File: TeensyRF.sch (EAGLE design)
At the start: 9 parts, among them X1 SMA-142-0701-801/806, X2 SMA-142-0701-801/806

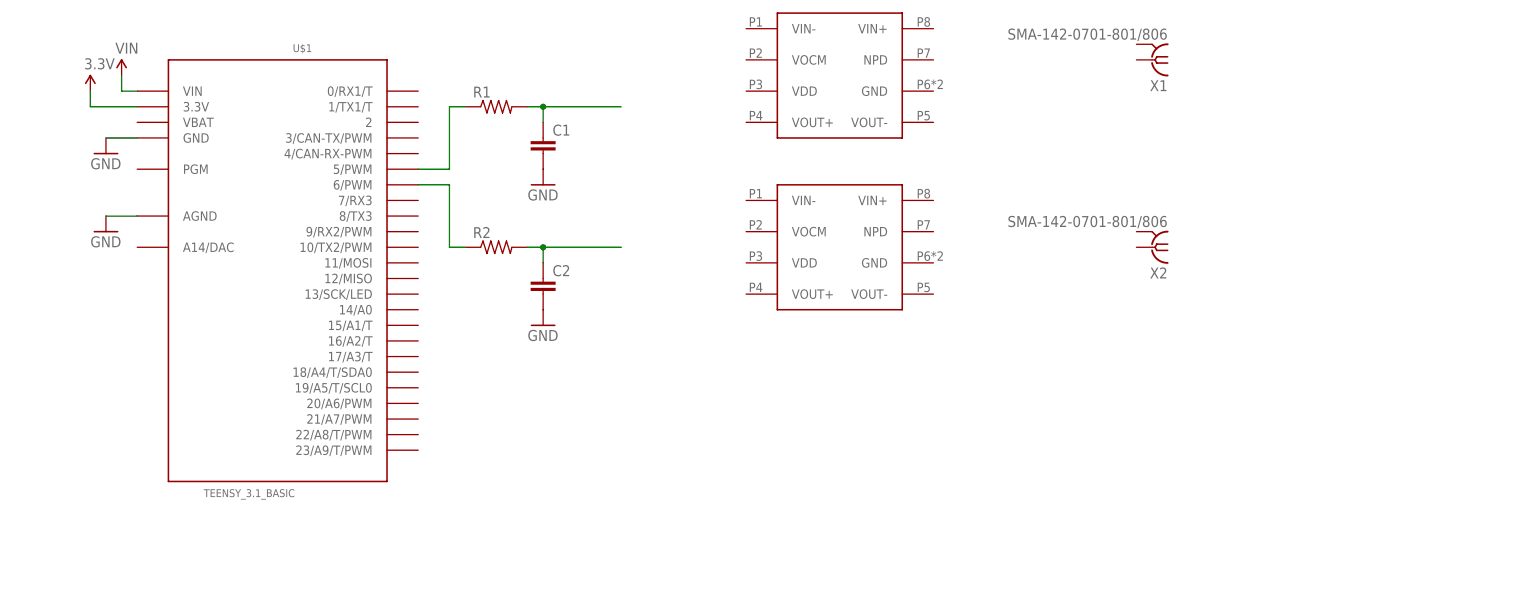
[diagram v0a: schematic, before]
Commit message: Finished TX schematic
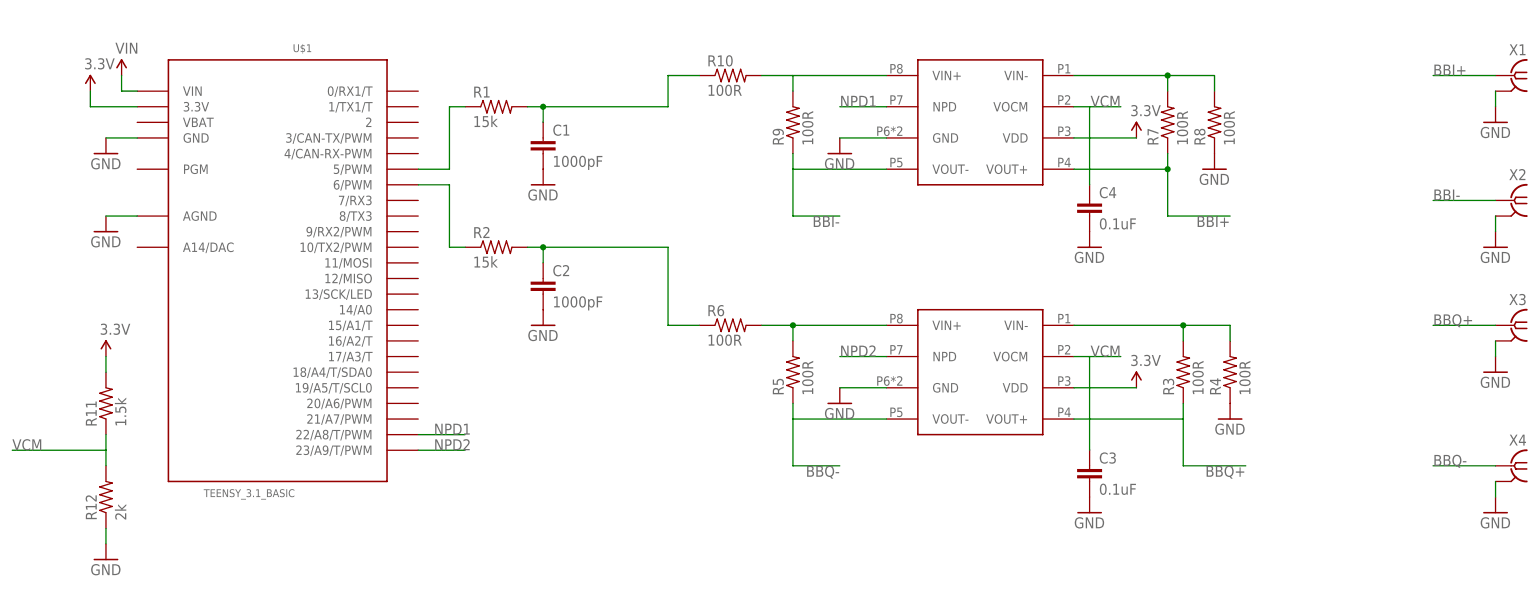
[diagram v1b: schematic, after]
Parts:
- added C3, C4: 0.1uF, SparkFun-Capacitors:CAP0805
- added R10, R3, R4, R5, R6, R7, R8, R9: 100R, SparkFun-Resistors:RESISTOR0805-RES
- added R11: 1.5k, SparkFun-Resistors:RESISTOR0805-RES
- added R12: 2k, SparkFun-Resistors:RESISTOR0805-RES
- added X3, X4: SMA-142-0701-801/806, con-coax:SMA-142-0701-801/806
- C1, C2: value (none) -> 1000pF
- R1, R2: value (none) -> 15k
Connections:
- new net BBI+: R7.1, U$2.VOUT+, X1.1
- new net BBI-: R9.1, U$2.VOUT-, X2.1
- new net BBQ+: R3.1, U$3.VOUT+, X3.1
- new net BBQ-: R5.1, U$3.VOUT-, X4.1
- new net N$11: R7.2, R8.2, U$2.VIN-
- new net N$13: R10.2, R9.2, U$2.VIN+
- new net N$6: R5.2, R6.2, U$3.VIN+
- new net N$8: R3.2, R4.2, U$3.VIN-
- new net NPD1: U$1.22/A8/T/PWM, U$2.NPD
- new net NPD2: U$1.23/A9/T/PWM, U$3.NPD
- new net VCM: C3.1, C4.1, R11.1, R12.2, U$2.VOCM, U$3.VOCM
- net 3.3V: now also R11.2, U$2.VDD, U$3.VDD
- net GND: now also C3.2, C4.2, R12.1, R4.1, R8.1, U$2.GND, U$3.GND, X1.2, X2.2, X3.2, X4.2
- net N$2: now also R10.1
- net N$4: now also R6.1
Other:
- moved on the sheet: X1, X2

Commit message: Finished TX Test board layout
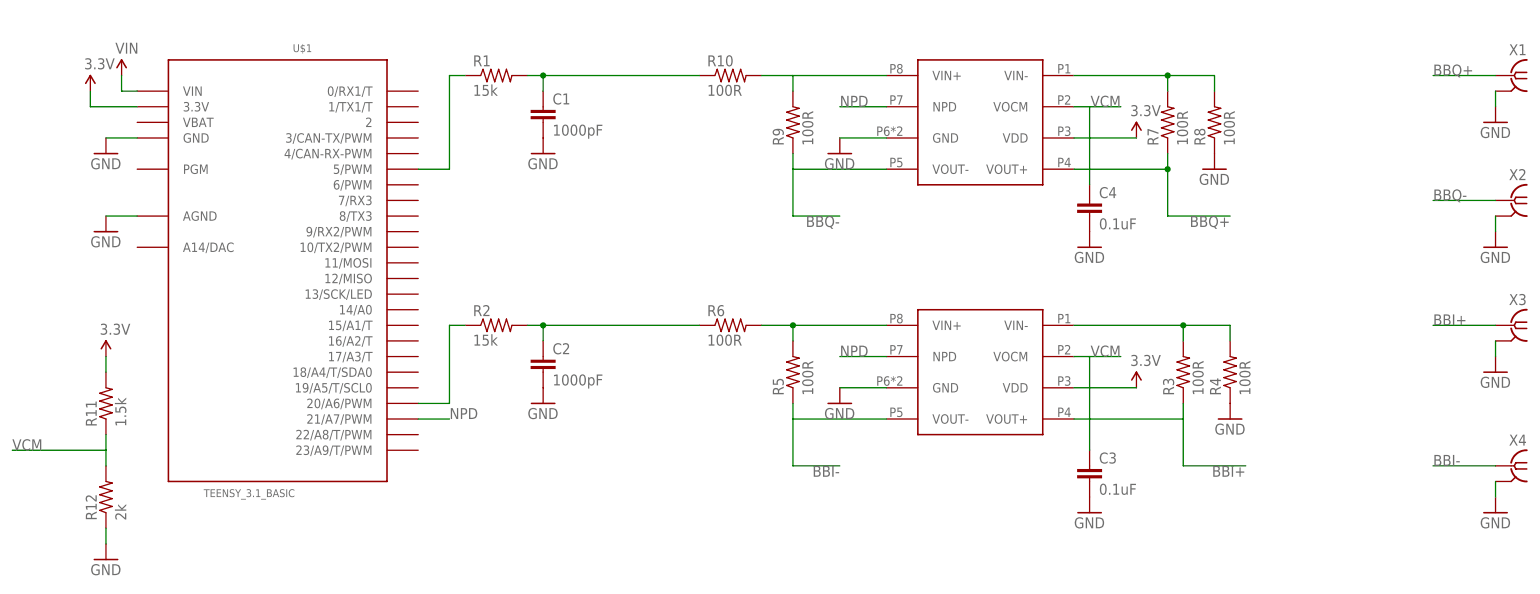
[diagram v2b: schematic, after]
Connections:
- removed net NPD1: U$1.22/A8/T/PWM, U$2.NPD
- removed net NPD2: U$1.23/A9/T/PWM, U$3.NPD
- new net NPD: U$1.21/A7/PWM, U$2.NPD, U$3.NPD
- net BBI+: now also R3.1, U$3.VOUT+, X3.1; no longer R7.1, U$2.VOUT+, X1.1
- net BBI-: now also R5.1, U$3.VOUT-, X4.1; no longer R9.1, U$2.VOUT-, X2.1
- net BBQ+: now also R7.1, U$2.VOUT+, X1.1; no longer R3.1, U$3.VOUT+, X3.1
- net BBQ-: now also R9.1, U$2.VOUT-, X2.1; no longer R5.1, U$3.VOUT-, X4.1
- net N$3: now also U$1.20/A6/PWM; no longer U$1.6/PWM
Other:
- moved on the sheet: C1, C2, R1, R2

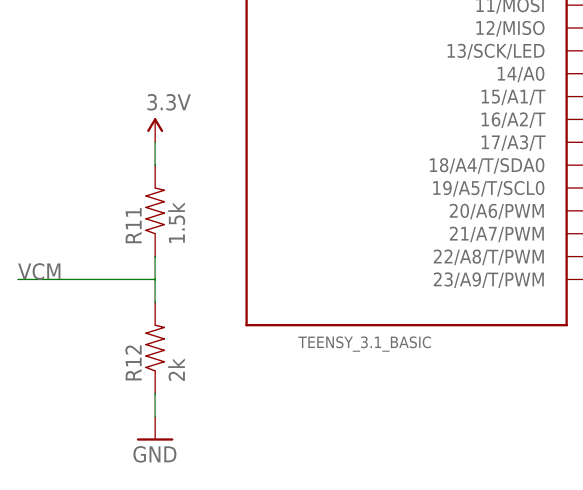
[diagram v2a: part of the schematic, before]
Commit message: Fixed R11 R12 mixup
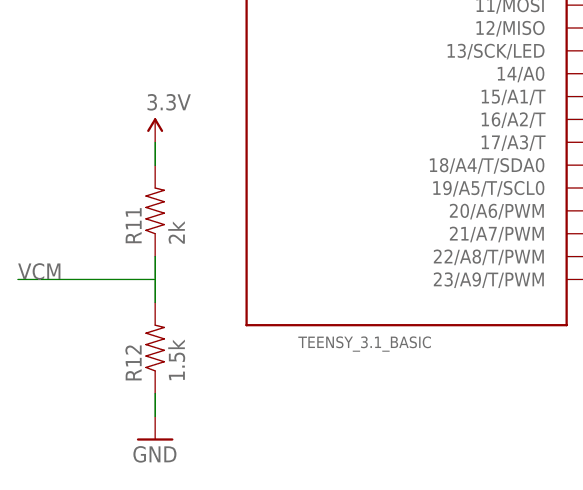
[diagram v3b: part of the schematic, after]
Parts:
- R11: value 1.5k -> 2k
- R12: value 2k -> 1.5k
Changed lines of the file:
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@@
 <part name="C4" library="SparkFun-Capacitors" deviceset="CAP" device="0805" value="0.1uF"/>
 <part name="GND10" library="SparkFun-Aesthetics" deviceset="GND" device=""/>
-<part name="R11" library="SparkFun-Resistors" deviceset="RESISTOR" device="0805-RES" value="1.5k"/>
-<part name="R12" library="SparkFun-Resistors" deviceset="RESISTOR" device="0805-RES" value="2k"/>
+<part name="R11" library="SparkFun-Resistors" deviceset="RESISTOR" device="0805-RES" value="2k"/>
+<part name="R12" library="SparkFun-Resistors" deviceset="RESISTOR" device="0805-RES" value="1.5k"/>
 <part name="SUPPLY5" library="SparkFun-Aesthetics" deviceset="3.3V" device=""/>
 <part name="GND11" library="SparkFun-Aesthetics" deviceset="GND" device=""/>
